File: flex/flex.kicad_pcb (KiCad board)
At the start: 2 copper layers, 47.2 x 41.5 mm, 18 parts, among them J1 Conn_01x06_Female, J2 Conn_01x03_Female, SW19 SW_Push, SW5 SW_Push, SW9 SW_Push

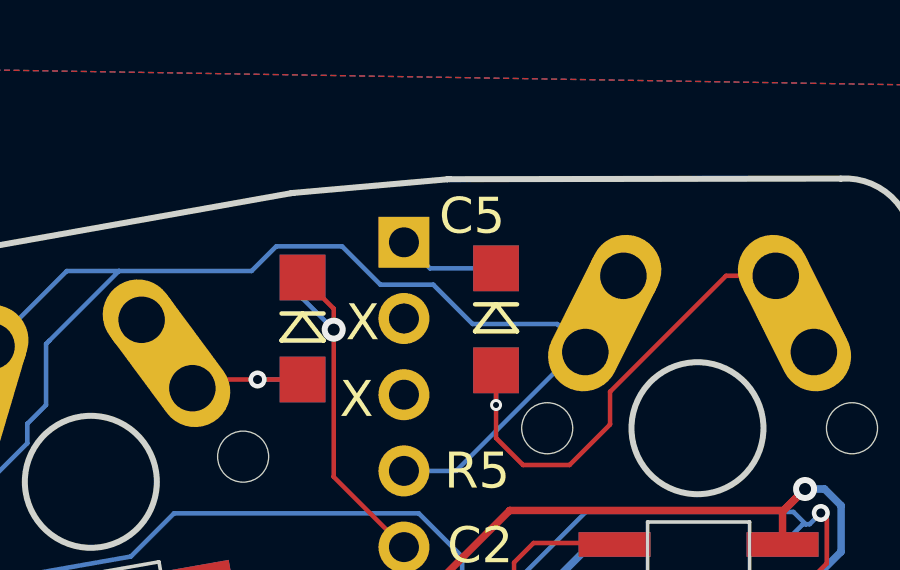
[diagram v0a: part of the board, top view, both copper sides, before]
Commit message: add missing diode route
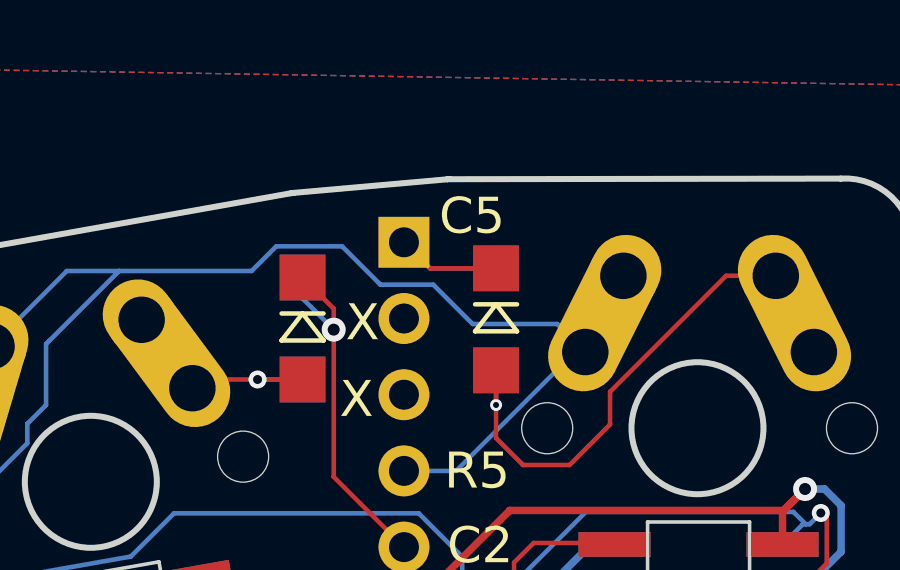
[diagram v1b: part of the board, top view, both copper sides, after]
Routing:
- net col5: track 3.43 -> 6.86 mm
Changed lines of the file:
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@@
   (via (at 87.5 73.8) (size 0.4) (drill 0.2) (layers "F.Cu" "B.Cu") (net 9))
   (segment (start 87.5 73.8) (end 87.5 72.644) (width 0.1524) (layer "B.Cu") (net 9))
+  (segment (start 87.5 69.244) (end 85.2968 69.244) (width 0.1524) (layer "F.Cu") (net 10))
+  (segment (start 85.2968 69.244) (end 84.4296 68.3768) (width 0.1524) (layer "F.Cu") (net 10))
   (segment (start 85.2968 69.244) (end 84.4296 68.3768) (width 0.1524) (layer "B.Cu") (net 10))
   (segment (start 87.5 69.244) (end 85.2968 69.244) (width 0.1524) (layer "B.Cu") (net 10))

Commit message: version
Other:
- board text added: "rev 1.2"
- board text removed: "rev 1.1"
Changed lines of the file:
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@@
     (effects (font (size 1.2 1.2) (thickness 0.2)) (justify mirror))
   )
-  (gr_text "rev 1.1" (at 89.55 92.6 90) (layer "B.SilkS")
+  (gr_text "rev 1.2" (at 89.55 92.6 90) (layer "B.SilkS")
     (effects (font (size 1.2 1.2) (thickness 0.2)) (justify mirror))
   )
@@
     (effects (font (size 1 1) (thickness 0.15)))
   )
-  (gr_text "rev 1.1" (at 89.65 92.700001 90) (layer "F.SilkS")
+  (gr_text "rev 1.2" (at 89.65 92.700001 90) (layer "F.SilkS")
     (effects (font (size 1.2 1.2) (thickness 0.2)))
   )

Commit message: make universal
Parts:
- removed C1, C2: C, LED_SMD:LED_1206_3216Metric_Pad1.42x1.75mm_HandSolder
- removed D10, D12, D2: SK6812MINI, libs2:YS-SK6812MINI-E_REVERSE
- removed D11, D13, D3: SK6812MINI, libs2:YS-SK6812MINI-E_REVERSE_NO_EDGECUT
- removed J2: Conn_01x03_Female, Connector_PinHeader_2.54mm:PinHeader_1x03_P2.54mm_Vertical
- removed R1, R2: R, Resistor_SMD:R_1206_3216Metric_Pad1.42x1.75mm_HandSolder
- moved D9 19.6 mm to (71.0, 102.8), turned to 0 degrees
- moved D5 18.6 mm to (69.6, 81.0), turned to 0 degrees
- moved D19 13.0 mm to (89.2, 78.8), turned to 0 degrees
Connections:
- D19 pad 1: col5 -> col4
- D9 pad 1: col3 -> col6
- J1 pad 1: col5 -> unconnected-(J1-Pad1)
- J1 pad 6: col3 -> unconnected-(J1-Pad6)
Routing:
- net Gnd: track 87.6 -> 0.00 mm, vias 4 -> 0
- net Vcc: track 85.4 -> 0.00 mm, vias 5 -> 0
- net Net-(D2-Pad1): track 67.4 -> 0.00 mm, vias 2 -> 0
- net col6: track 0.00 -> 48.7 mm, vias 0 -> 1
- net Net-(D10-Pad1): track 47.5 -> 0.00 mm, vias 3 -> 0
- net Net-(D2-Pad3): track 24.9 -> 0.00 mm, vias 2 -> 0
- net col3: track 22.5 -> 0.00 mm, vias 1 -> 0
- net col4: track 0.00 -> 12.3 mm, vias 0 -> 1
- net Net-(D5-Pad2): track 5.29 -> 16.3 mm, vias 1 -> 0
- net col5: track 6.86 -> 0.00 mm
- net Din: track 6.35 -> 0.00 mm
- net col2: track 12.6 -> 15.2 mm
- net Net-(D9-Pad2): track 9.04 -> 10.1 mm
- net Net-(D19-Pad2): track 16.4 -> 15.5 mm, vias 1 -> 0
- added copper zone on B.Cu, net (none)
- added copper zone on F.Cu, net (none)
- removed copper zone on B.Cu, net Gnd
- removed copper zone on F.Cu, net Gnd
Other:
- board text added: "C4"
- board text added: "C6"
- board text added: "Mini"
- board text added: "rev 1.3"
- board text removed: "C"
- board text removed: "Din"
- board text removed: "Gnd"
- board text removed: "R"
- board text removed: "Vcc"
- board text removed: "X"
- board text removed: "rev 1.2"

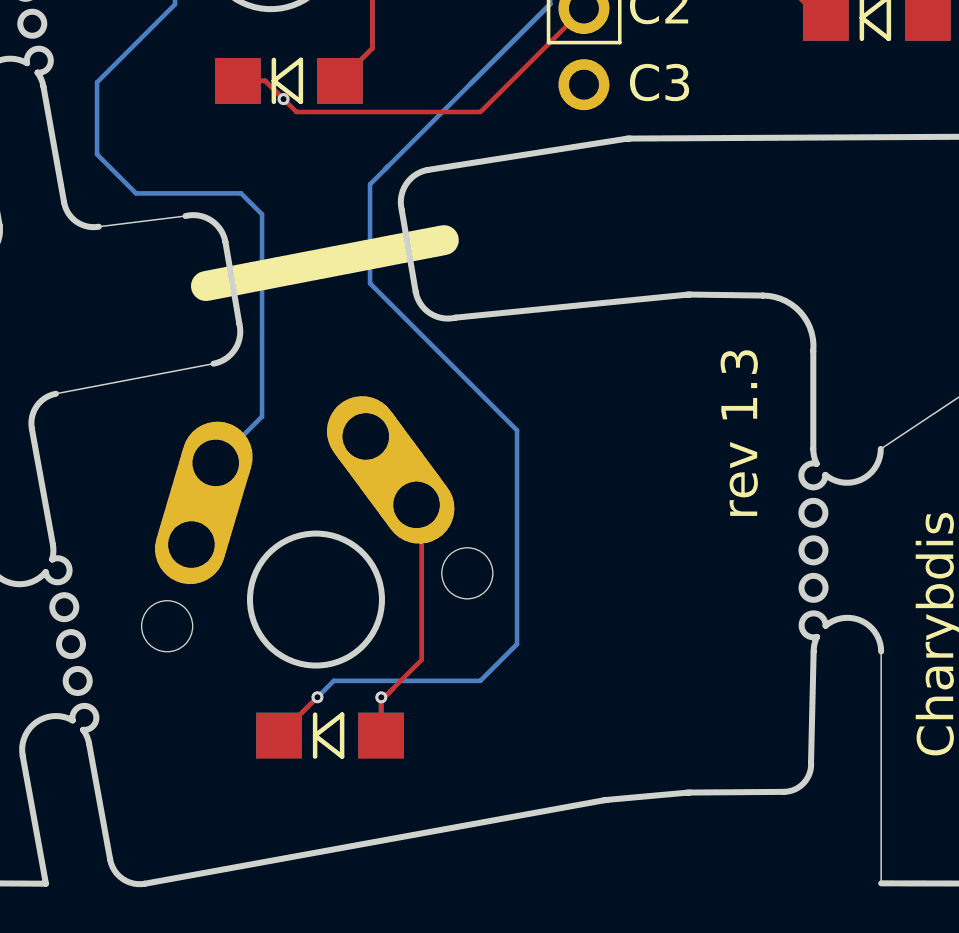
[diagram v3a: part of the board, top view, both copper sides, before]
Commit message: ad right/left
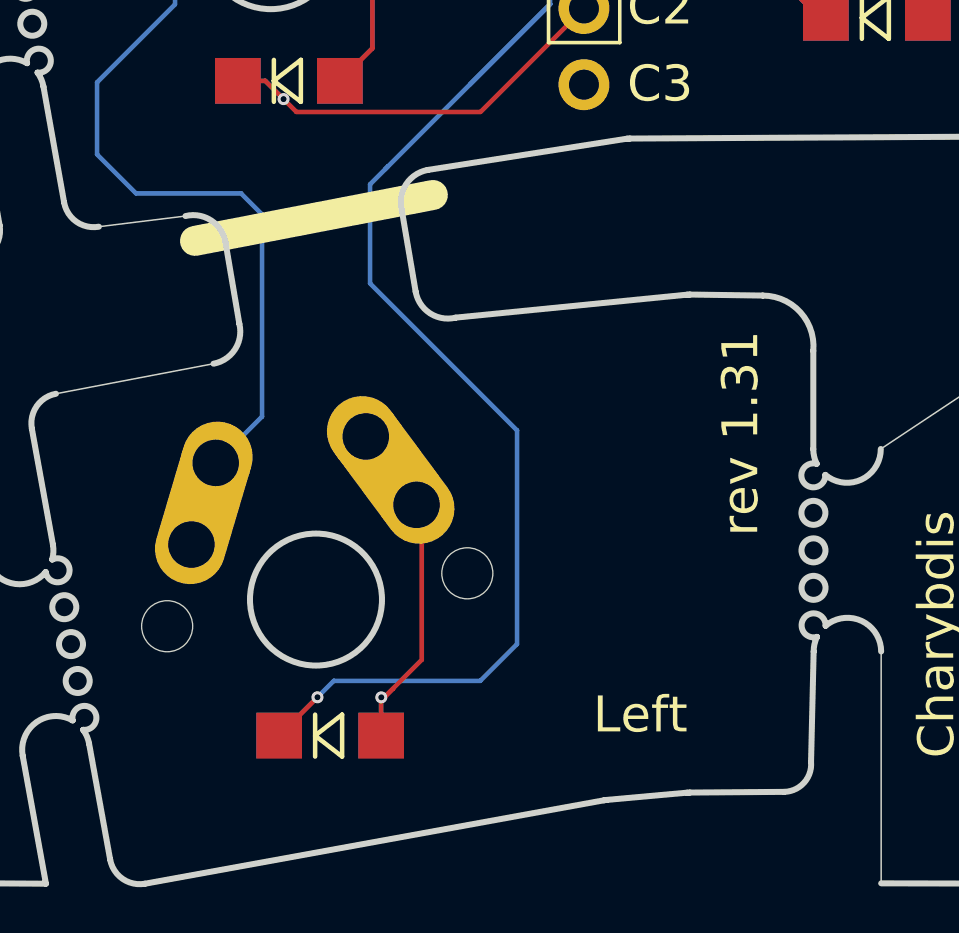
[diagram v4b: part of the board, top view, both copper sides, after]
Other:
- board text added: "Left"
- board text added: "Right"
- board text added: "rev 1.31"
- board text removed: "rev 1.3"
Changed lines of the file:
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@@
       (net 2 "Net-(D5-Pad2)") (pinfunction "2") (pintype "passive"))
   )
-  (gr_line (start 79.625 86.25) (end 71.2 87.9) (layer "B.SilkS") (width 1))
+  (gr_line (start 79.26 84.745) (end 70.835 86.395) (layer "B.SilkS") (width 1))
   (gr_rect (start 83.2475 79.675) (end 85.6225 69.725) (layer "B.SilkS") (width 0.12) (fill none))
   (gr_rect (start 83.25 69.725) (end 85.625 79.675) (layer "F.SilkS") (width 0.12) (fill none))
-  (gr_line (start 79.76 86.26) (end 71.83 87.79) (layer "F.SilkS") (width 1))
+  (gr_line (start 79.395 84.755) (end 71.465 86.285) (layer "F.SilkS") (width 1))
   (gr_arc (start 102.625001 81.223028) (end 101.612082 80.733521) (angle -25.89275579) (layer "Edge.Cuts") (width 0.2))
   (gr_arc (start 102.61322 74.473039) (end 101.889442 75.334299) (angle -130.1427885) (layer "Edge.Cuts") (width 0.2))
@@
     (effects (font (size 1.2 1.2) (thickness 0.2)) (justify mirror))
   )
-  (gr_text "rev 1.3" (at 89.55 92.6 90) (layer "B.SilkS")
+  (gr_text "rev 1.31" (at 89.55 92.6 90) (layer "B.SilkS")
+    (effects (font (size 1.2 1.2) (thickness 0.2)) (justify mirror))
+  )
+  (gr_text "Right" (at 86.37 102.11) (layer "B.SilkS")
     (effects (font (size 1.2 1.2) (thickness 0.2)) (justify mirror))
   )
@@
     (effects (font (size 1.2 1.2) (thickness 0.2)))
   )
-  (gr_text "rev 1.3" (at 89.65 92.700001 90) (layer "F.SilkS")
+  (gr_text "rev 1.31" (at 89.65 92.700001 90) (layer "F.SilkS")
     (effects (font (size 1.2 1.2) (thickness 0.2)))
   )
@@
     (effects (font (size 1.2 1.2) (thickness 0.2)))
   )
+  (gr_text "Left" (at 86.309999 102.08) (layer "F.SilkS")
+    (effects (font (size 1.2 1.2) (thickness 0.2)))
+  )

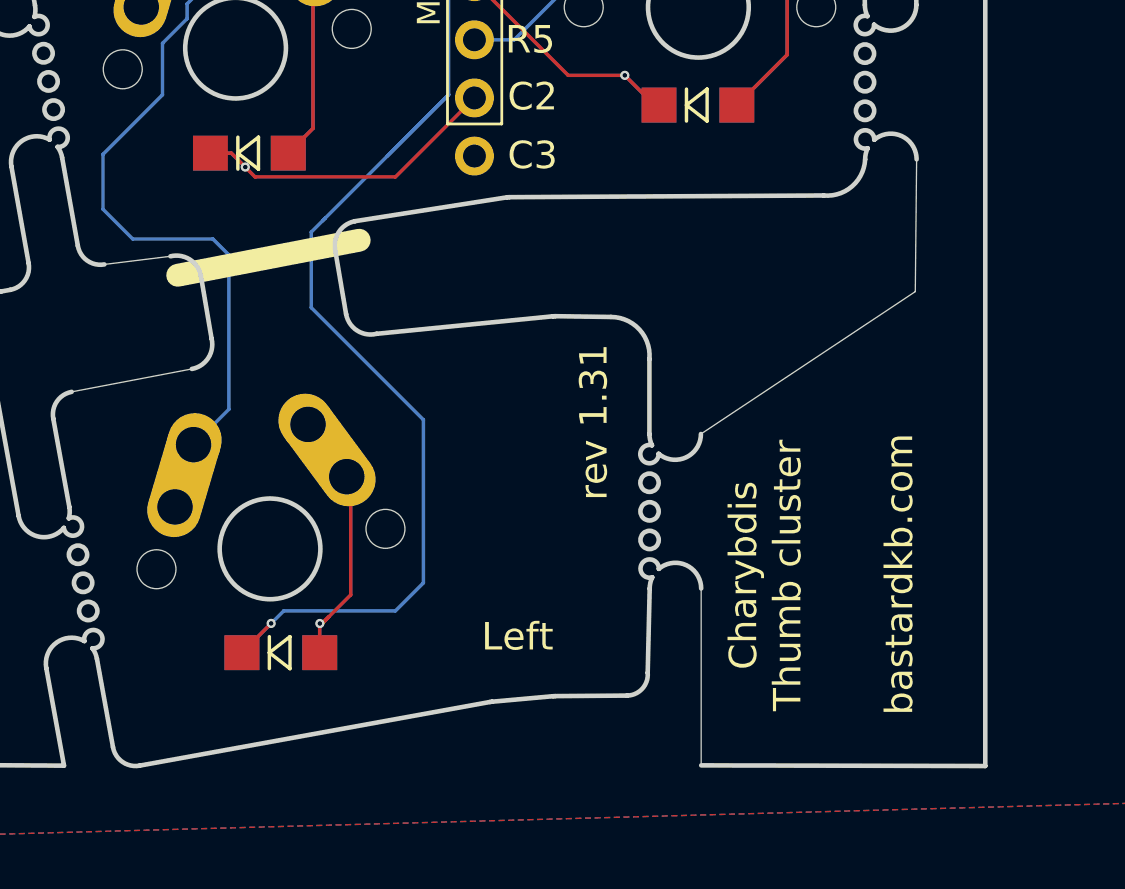
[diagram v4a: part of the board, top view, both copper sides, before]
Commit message: make bottom key smaller
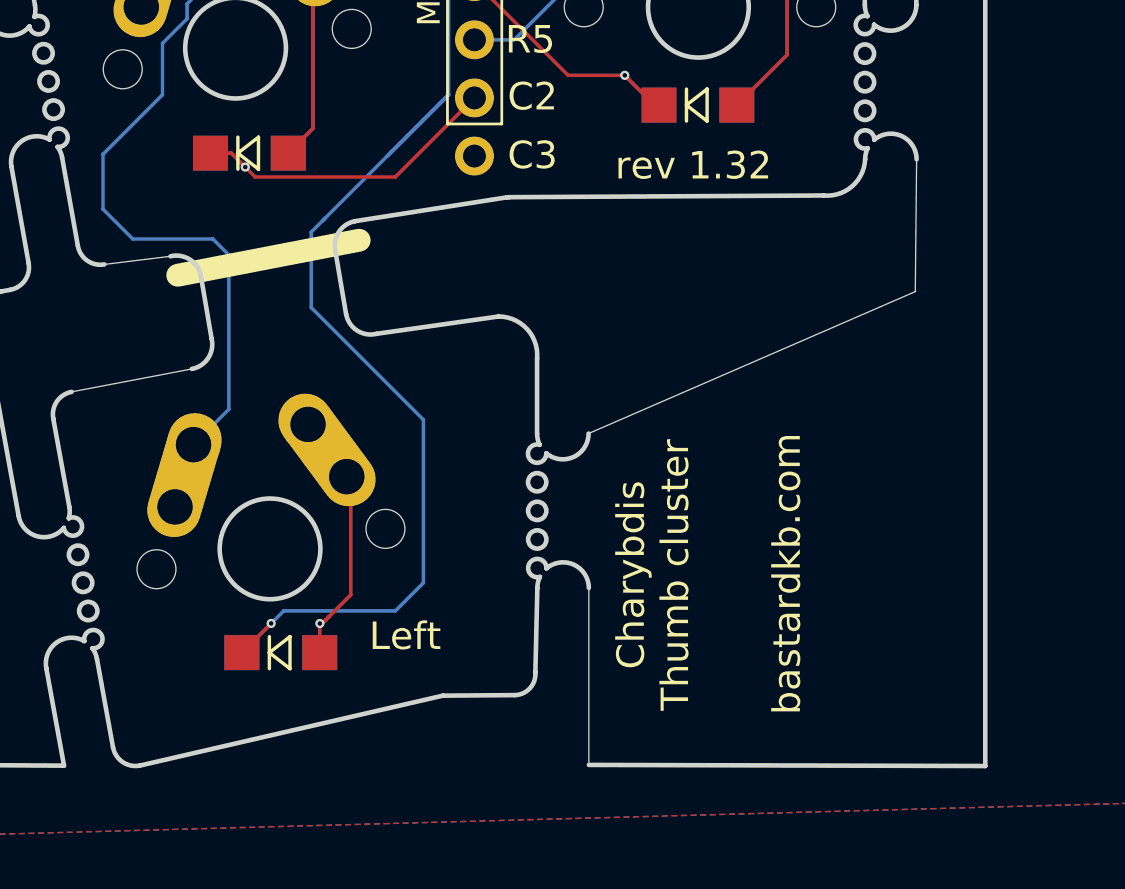
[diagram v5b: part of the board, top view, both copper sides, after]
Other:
- outline, holes or cut-outs redrawn
- board text added: "rev 1.32"
- board text removed: "rev 1.31"

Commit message: silkscreen
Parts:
- added G***: LOGO, LOGO, F.Cu at (95.8, 98.0)
- added G***: LOGO, LOGO, B.Cu at (95.9, 98.0)
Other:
- board text added: "3 ROWS"
- board text added: "BASTARDKB.COM"
- board text added: "C2R5"
- board text added: "C3R5"
- board text added: "C5R5"
- board text added: "CHARYBDIS THUMB CLUSTER"
- board text added: "GITHUB.COM/BASTARDKB"
- board text added: "LEFT"
- board text added: "REV 1.33"
- board text added: "RIGHT"
- board text removed: "Charybdis Thumb cluster"
- board text removed: "Left"
- board text removed: "Mini"
- board text removed: "Right"
- board text removed: "bastardkb.com"
- board text removed: "rev 1.32"

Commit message: add rgb
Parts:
- removed the G*** at (95.8, 98.0)
- removed the G*** at (95.9, 98.0)
- added C1: C, LED_SMD:LED_1206_3216Metric_Pad1.42x1.75mm_HandSolder, F.Cu at (67.2, 80.9)
- added C2: C, LED_SMD:LED_1206_3216Metric_Pad1.42x1.75mm_HandSolder, B.Cu at (67.2, 80.9)
- added D10: SK6812MINI, libs2:YS-SK6812MINI-E_REVERSE, F.Cu at (94.2, 79.2)
- added D11: SK6812MINI, libs2:YS-SK6812MINI-E_REVERSE_NO_EDGECUT, B.Cu at (94.2, 79.2)
- added D12: SK6812MINI, libs2:YS-SK6812MINI-E_REVERSE, F.Cu at (74.8, 80.8)
- added D13: SK6812MINI, libs2:YS-SK6812MINI-E_REVERSE_NO_EDGECUT, B.Cu at (74.8, 80.8)
- added D2: SK6812MINI, libs2:YS-SK6812MINI-E_REVERSE, F.Cu at (76.5, 102.8)
- added D3: SK6812MINI, libs2:YS-SK6812MINI-E_REVERSE_NO_EDGECUT, B.Cu at (76.5, 102.8)
- added G***: LOGO, LOGO, F.Cu at (95.9, 100.7)
- added G***: LOGO, LOGO, B.Cu at (96.0, 100.7)
- added J2: Conn_01x03_Female, Connector_PinHeader_2.54mm:PinHeader_1x03_P2.54mm_Vertical, F.Cu at (65.5, 71.6)
- added R1: R, Resistor_SMD:R_1206_3216Metric_Pad1.42x1.75mm_HandSolder, B.Cu at (81.1, 79.1)
- added R2: R, Resistor_SMD:R_1206_3216Metric_Pad1.42x1.75mm_HandSolder, F.Cu at (81.2, 79.2)
- moved D9 19.6 mm to (83.9, 88.0), turned to -90 degrees
- moved D5 18.2 mm to (80.7, 66.5), turned to -90 degrees
- moved D19 11.4 mm to (99.7, 74.5), turned to -90 degrees
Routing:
- net Vcc: track 0.00 -> 87.1 mm, vias 0 -> 4
- net Gnd: track 0.00 -> 77.7 mm, vias 0 -> 4
- net Net-(D10-Pad1): track 0.00 -> 69.9 mm, vias 0 -> 3
- net Net-(D12-Pad1): track 0.00 -> 28.0 mm, vias 0 -> 3
- net Din: track 0.00 -> 26.4 mm, vias 0 -> 1
- net Net-(D12-Pad3): track 0.00 -> 19.5 mm, vias 0 -> 3
- net Net-(D5-Pad2): track 16.3 -> 6.63 mm
- net col4: track 12.3 -> 20.2 mm
- net col6: track 48.7 -> 56.4 mm, vias 1 -> 3
- net row1: track 62.8 -> 57.9 mm, vias 0 -> 2
- net col2: track 15.2 -> 12.7 mm
- net Net-(D19-Pad2): track 15.5 -> 13.1 mm, vias 0 -> 1
- net Net-(D9-Pad2): track 10.1 -> 8.50 mm
- added copper zone on B.Cu, net Gnd
- added copper zone on F.Cu, net Gnd
- removed copper zone on B.Cu, net (none)
- removed copper zone on F.Cu, net (none)
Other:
- board size 47.2 x 41.5 mm -> 48.8 x 41.5 mm
- board text added: "C"
- board text added: "Conn_01x02_Female"
- board text added: "Conn_01x06_Female"
- board text added: "Din"
- board text added: "R"
- board text added: "REV 2.0"
- board text added: "Vcc"
- board text removed: "REV 1.33"

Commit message: add licenses
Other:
- board text added: "Licensed under CC BY-NC-SA 4.0 Copyright Quentin Lebastard 2022"
- board text added: "REV 2.01"
- board text removed: "Din"
- board text removed: "REV 2.0"
